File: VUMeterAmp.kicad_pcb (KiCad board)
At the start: 2 copper layers, 86 x 40 mm, 80 parts, among them J1 Conn_01x03, J2 Conn_01x03, J3 Conn_01x07, J4 Conn_01x07, J5 Conn_01x03, J6 Conn_01x02, J7 Conn_02x04_Top_Bottom, SW1 SW_DPST_x2, SW2 SW_SPST, U1 NJM4580, U2 NJM4580, U3 NJM4580

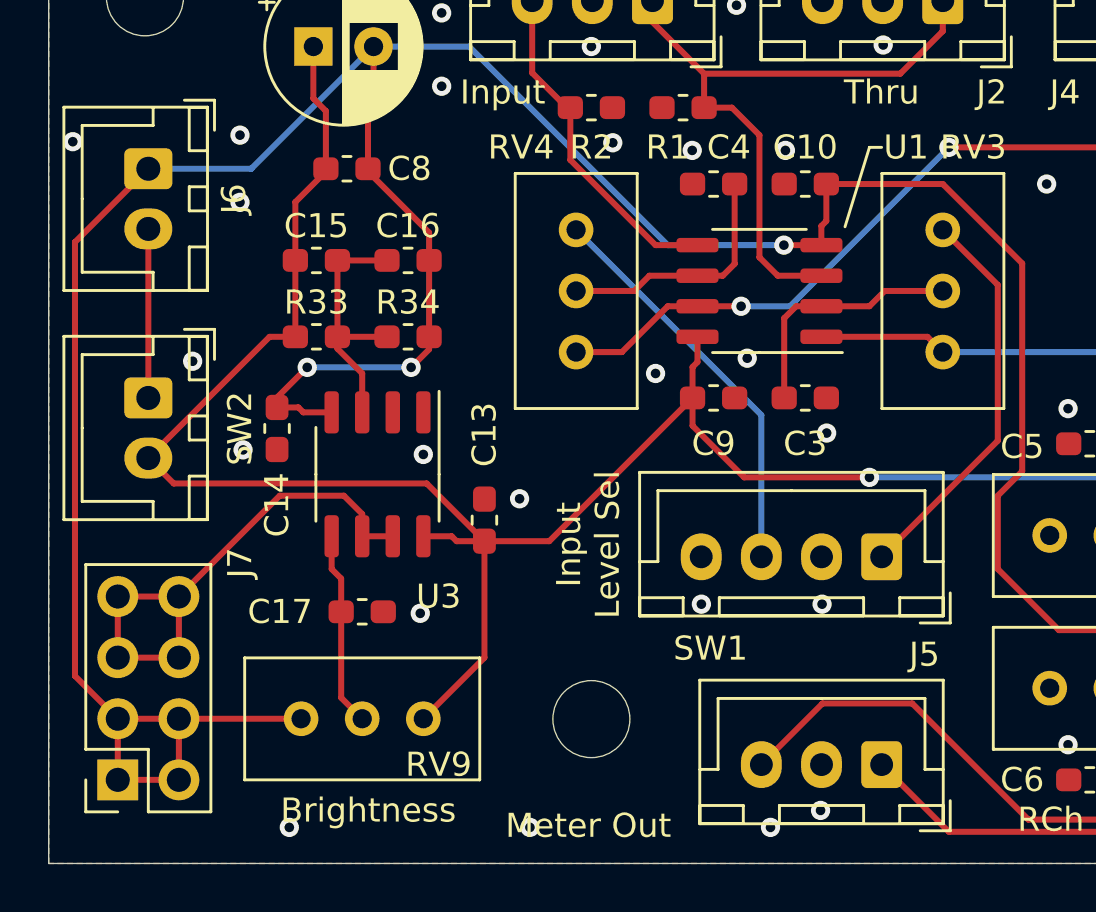
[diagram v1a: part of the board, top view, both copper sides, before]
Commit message: delete light
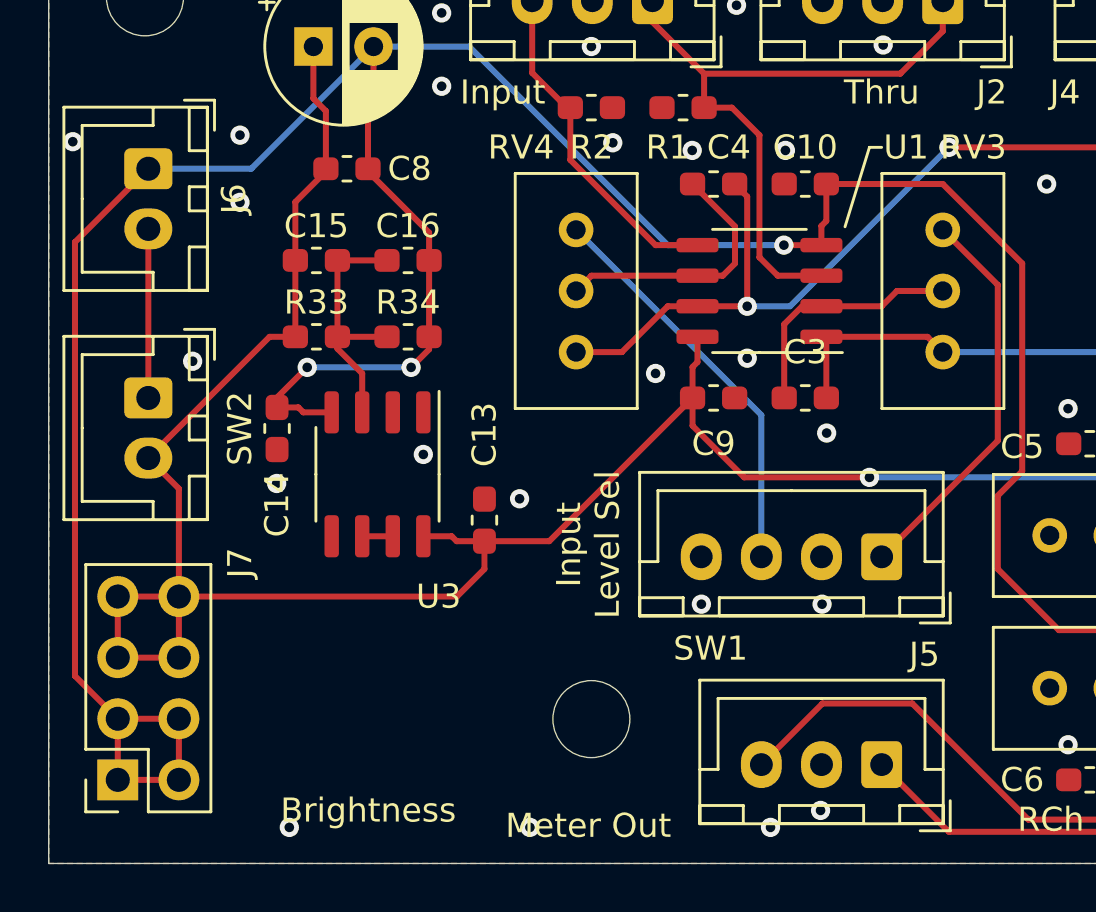
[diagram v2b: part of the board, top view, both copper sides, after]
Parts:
- removed C17: 0.1u, Capacitor_SMD:C_0603_1608Metric_Pad1.05x0.95mm_HandSolder
- removed G***: LOGO, toripoyo:tiemi2
- removed RV9: 10k, Potentiometer_THT:Potentiometer_Bourns_3296W_Vertical
- turned C3 to 180 degrees
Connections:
- C3 pad 2: GND -> Net-(C3-Pad2)
- C4 pad 2: GND -> Net-(C4-Pad2)
- J7 pad 5: Net-(J7-Pad5) -> Power_Pos
- J7 pad 6: Net-(J7-Pad5) -> Power_Pos
- J7 pad 7: Net-(J7-Pad5) -> Power_Pos
- J7 pad 8: Net-(J7-Pad5) -> Power_Pos
- R3 pad 2: Net-(R3-Pad2) -> Net-(C3-Pad1)
- R4 pad 2: Net-(R4-Pad2) -> Net-(C4-Pad1)
- RV3 pad 2: Net-(C3-Pad1) -> Net-(C3-Pad2)
- RV3 pad 3: Net-(R3-Pad2) -> Net-(C3-Pad1)
- RV4 pad 2: Net-(C4-Pad1) -> Net-(C4-Pad2)
- RV4 pad 3: Net-(R4-Pad2) -> Net-(C4-Pad1)
- U1 pad 1: Net-(R3-Pad2) -> Net-(C3-Pad1)
- U1 pad 2: Net-(C3-Pad1) -> Net-(C3-Pad2)
- U1 pad 6: Net-(C4-Pad1) -> Net-(C4-Pad2)
- U1 pad 7: Net-(R4-Pad2) -> Net-(C4-Pad1)
- U3 pad 5: Net-(C17-Pad1) -> GND
- U3 pad 6: Net-(J7-Pad5) -> Net-(U3-Pad6)
- U3 pad 7: Net-(J7-Pad5) -> Net-(U3-Pad6)
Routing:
- net Net-(R3-Pad2): track 38.7 -> 0.00 mm, vias 1 -> 0
- net Net-(C3-Pad1): track 10.4 -> 41.4 mm, vias 0 -> 1
- net Net-(R4-Pad2): track 25.8 -> 0.00 mm, vias 2 -> 0
- net Net-(J7-Pad5): track 22.0 -> 0.00 mm
- net Net-(C4-Pad1): track 10.4 -> 31.1 mm, vias 0 -> 2
- net Net-(C4-Pad2): track 0.00 -> 11.1 mm
- net Net-(C3-Pad2): track 0.00 -> 10.2 mm
- net Net-(C17-Pad1): track 8.11 -> 0.00 mm
- net Power_Pos: track 126.1 -> 133.0 mm
- net Power_Neg: track 175.4 -> 170.3 mm
- net Net-(U3-Pad6): track 0.00 -> 1.27 mm
- net GND: vias 72 -> 71
